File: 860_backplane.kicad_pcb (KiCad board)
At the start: 4 copper layers, 38 x 106 mm, 7 parts, among them P1 CONN_02X05

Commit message: silk screen adjust on 860 PCB, alignment check of backplane: OK
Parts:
- added G***: LOGO, Logos:860_CPU_backplane, B.Cu at (122.9, 69.2)

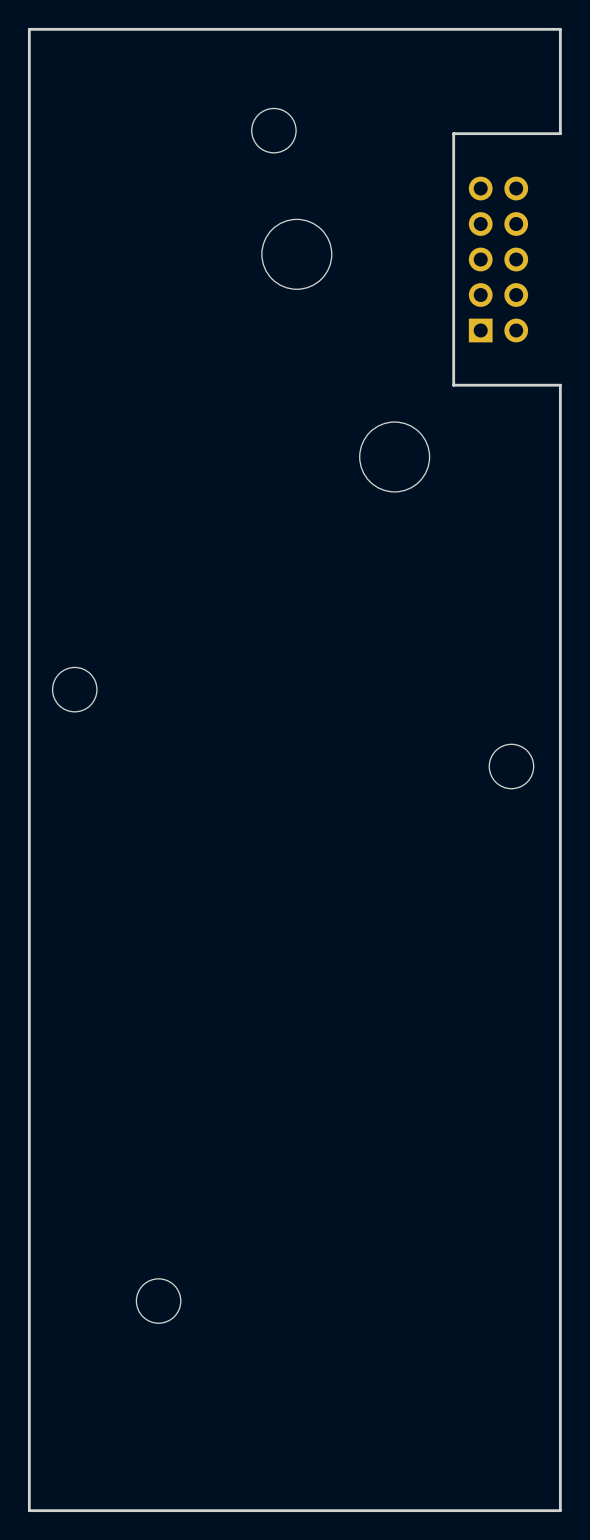
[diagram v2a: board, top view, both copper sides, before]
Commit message: ordered next revision PCB for testing, fitting, added backplane
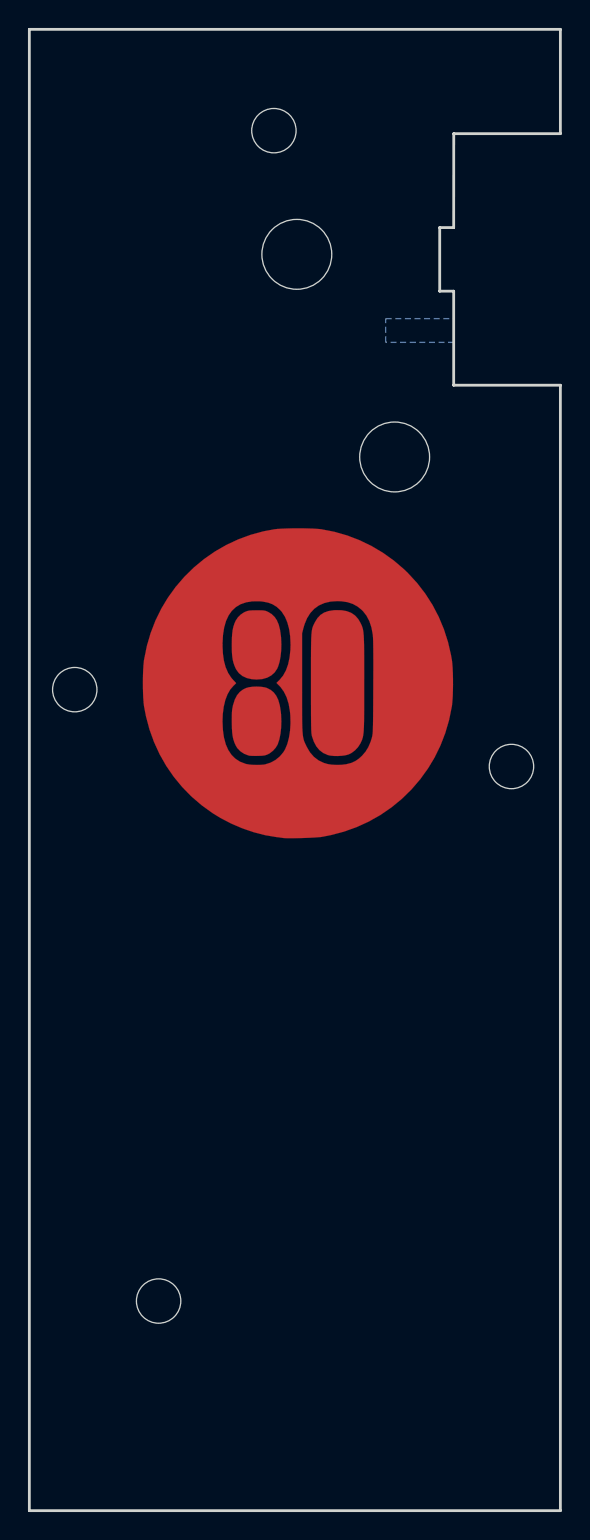
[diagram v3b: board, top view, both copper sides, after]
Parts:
- removed P1: CONN_02X05, Pin_Headers:Pin_Header_Straight_2x05_Pitch2.54mm
- added G***: LOGO, Logos:80_logo_Fcu, F.Cu at (123.1, 63.0)
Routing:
- added copper zone on B.Cu, net (none)
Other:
- outline, holes or cut-outs redrawn
- copper layers 4 -> 2
